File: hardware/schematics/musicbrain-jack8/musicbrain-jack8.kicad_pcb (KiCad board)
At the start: 2 copper layers, 20 x 125 mm, 10 parts, among them J1 SOCKET-BACK, J2 PJ398SM, J3 PJ398SM, J4 PJ398SM, J5 PJ398SM, J6 PJ398SM, J7 PJ398SM, J8 PJ398SM, J9 PJ398SM

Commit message: jack8/jack4 v1.2 + pot8front v1.1: koppel-standaard + 3D-socket-fix
- Front-koppeling gestandaardiseerd: 1x10-socket op x=116,5 (16,5 van west-
  rand), pin 1 op y=143,57 - identiek op jack8, jack4 en pot8front
- B-zijde-sockets nu in KiCads canonieke geflipte vorm (rot 180, lokale y
  genegeerd): koper ongewijzigd, maar het 3D-model staat nu OP de gatenrij
  i.p.v. ernaast gespiegeld
- PCB-papier naar A3 (borden vielen van A4-landscape af), silk-URL naar
  bordmidden (viel over de bordrand door center-justify)
- make_fab.sh: bordenlijst actueel (deprecated eruit, fronts erin),
  selectie-argument + gerber-zip-stap toegevoegd
- ERC/netcheck/DRC 0/0 op alle drie; fab + PDF's ververst

Co-Authored-By: Claude Fable 5 <noreply@anthropic.com>
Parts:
- moved J1 7.65 mm to (116.5, 143.6), turned to 180 degrees
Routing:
- net /CH8: track 43.7 -> 52.7 mm
- net /CH7: track 31.2 -> 40.2 mm
- net /CH6: track 18.8 -> 27.8 mm
- net /CH5: track 7.69 -> 15.3 mm
- net /CH4: track 20.1 -> 14.1 mm
- net /CH3: track 32.6 -> 26.6 mm
- net /CH2: track 45.1 -> 39.1 mm
- net /CH1: track 57.5 -> 51.5 mm
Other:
- board text added: "musicbrain.nl/hw/jack8 rev 1.2"
- board text removed: "musicbrain.nl/hw/jack8 rev 1.1"
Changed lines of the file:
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@@
   (generator_version "8.0")
   (general (thickness 1.6) (legacy_teardrops no))
-  (paper "A4")
+  (paper "A3")
   (title_block
     (title "MusicBrain jack8")
-    (date "2026-07-08")
-    (rev "1.1")
+    (date "2026-07-11")
+    (rev "1.2")
     (company "MusicBrain project")
   )
@@
   (footprint "MusicBrain:Header_1x10_backside"
     (layer "B.Cu")
-    (at 115 151.07)
+    (at 116.5 143.57 180)
     (descr "1x10 female socket op de ACHTERZIJDE (opening omlaag, naar de kaart)")
-    (property "Reference" "J1" (at 2.8 -2.2 0) (layer "B.SilkS")
+    (property "Reference" "J1" (at -2.8 2.2 0) (layer "B.SilkS")
       (effects (font (size 1 1) (thickness 0.15)) (justify mirror)))
-    (property "Value" "SOCKET-BACK" (at 0 25.86 0) (layer "B.Fab")
+    (property "Value" "SOCKET-BACK" (at 0 -25.86 0) (layer "B.Fab")
       (effects (font (size 1 1) (thickness 0.15)) (justify mirror)))
     (attr through_hole)
-    (fp_rect (start -1.6 -1.6) (end 1.6 24.46)
+    (fp_rect (start -1.6 -24.46) (end 1.6 1.6)
       (stroke (width 0.12) (type solid)) (fill no) (layer "B.SilkS"))
-    (fp_rect (start -1.8 -1.8) (end 1.8 24.66)
+    (fp_rect (start -1.8 -24.66) (end 1.8 1.8)
       (stroke (width 0.05) (type solid)) (fill no) (layer "B.CrtYd"))
-    (pad "1" thru_hole rect (at 0 0) (size 1.7 1.7) (drill 1.0) (layers "*.Cu" "*.Mask") (net 1 "GND"))
-    (pad "2" thru_hole oval (at 0 2.54) (size 1.7 1.7) (drill 1.0) (layers "*.Cu" "*.Mask") (net 3 "/CH1"))
-    (pad "3" thru_hole oval (at 0 5.08) (size 1.7 1.7) (drill 1.0) (layers "*.Cu" "*.Mask") (net 4 "/CH2"))
-    (pad "4" thru_hole oval (at 0 7.62) (size 1.7 1.7) (drill 1.0) (layers "*.Cu" "*.Mask") (net 5 "/CH3"))
-    (pad "5" thru_hole oval (at 0 10.16) (size 1.7 1.7) (drill 1.0) (layers "*.Cu" "*.Mask") (net 6 "/CH4"))
-    (pad "6" thru_hole oval (at 0 12.7) (size 1.7 1.7) (drill 1.0) (layers "*.Cu" "*.Mask") (net 7 "/CH5"))
-    (pad "7" thru_hole oval (at 0 15.24) (size 1.7 1.7) (drill 1.0) (layers "*.Cu" "*.Mask") (net 8 "/CH6"))
-    (pad "8" thru_hole oval (at 0 17.78) (size 1.7 1.7) (drill 1.0) (layers "*.Cu" "*.Mask") (net 9 "/CH7"))
-    (pad "9" thru_hole oval (at 0 20.32) (size 1.7 1.7) (drill 1.0) (layers "*.Cu" "*.Mask") (net 10 "/CH8"))
-    (pad "10" thru_hole oval (at 0 22.86) (size 1.7 1.7) (drill 1.0) (layers "*.Cu" "*.Mask") (net 1 "GND"))
+    (pad "1" thru_hole rect (at 0 -0 180) (size 1.7 1.7) (drill 1.0) (layers "*.Cu" "*.Mask") (net 1 "GND"))
+    (pad "2" thru_hole oval (at 0 -2.54 180) (size 1.7 1.7) (drill 1.0) (layers "*.Cu" "*.Mask") (net 3 "/CH1"))
+    (pad "3" thru_hole oval (at 0 -5.08 180) (size 1.7 1.7) (drill 1.0) (layers "*.Cu" "*.Mask") (net 4 "/CH2"))
+    (pad "4" thru_hole oval (at 0 -7.62 180) (size 1.7 1.7) (drill 1.0) (layers "*.Cu" "*.Mask") (net 5 "/CH3"))
+    (pad "5" thru_hole oval (at 0 -10.16 180) (size 1.7 1.7) (drill 1.0) (layers "*.Cu" "*.Mask") (net 6 "/CH4"))
+    (pad "6" thru_hole oval (at 0 -12.7 180) (size 1.7 1.7) (drill 1.0) (layers "*.Cu" "*.Mask") (net 7 "/CH5"))
+    (pad "7" thru_hole oval (at 0 -15.24 180) (size 1.7 1.7) (drill 1.0) (layers "*.Cu" "*.Mask") (net 8 "/CH6"))
+    (pad "8" thru_hole oval (at 0 -17.78 180) (size 1.7 1.7) (drill 1.0) (layers "*.Cu" "*.Mask") (net 9 "/CH7"))
+    (pad "9" thru_hole oval (at 0 -20.32 180) (size 1.7 1.7) (drill 1.0) (layers "*.Cu" "*.Mask") (net 10 "/CH8"))
+    (pad "10" thru_hole oval (at 0 -22.86 180) (size 1.7 1.7) (drill 1.0) (layers "*.Cu" "*.Mask") (net 1 "GND"))
     (model "${KICAD10_3DMODEL_DIR}/Connector_PinSocket_2.54mm.3dshapes/PinSocket_1x10_P2.54mm_Vertical.step"
       (offset (xyz 0 0 0)) (scale (xyz 1 1 1)) (rotate (xyz 0 0 0)))
@@
       (net 1 "GND"))
   )
-  (segment (start 115 153.61) (end 112.05 153.61) (width 0.25) (layer "F.Cu") (net 3))
-  (segment (start 112.05 153.61) (end 112.05 103.08) (width 0.25) (layer "F.Cu") (net 3))
-  (segment (start 112.05 103.08) (end 108 103.08) (width 0.25) (layer "F.Cu") (net 3))
-  (segment (start 115 156.15) (end 111.55 156.15) (width 0.25) (layer "F.Cu") (net 4))
-  (segment (start 111.55 156.15) (end 111.55 118.08) (width 0.25) (layer "F.Cu") (net 4))
-  (segment (start 111.55 118.08) (end 108 118.08) (width 0.25) (layer "F.Cu") (net 4))
-  (segment (start 115 158.69) (end 111.05 158.69) (width 0.25) (layer "F.Cu") (net 5))
-  (segment (start 111.05 158.69) (end 111.05 133.08) (width 0.25) (layer "F.Cu") (net 5))
-  (segment (start 111.05 133.08) (end 108 133.08) (width 0.25) (layer "F.Cu") (net 5))
-  (segment (start 115 161.23) (end 110.55 161.23) (width 0.25) (layer "F.Cu") (net 6))
-  (segment (start 110.55 161.23) (end 110.55 148.08) (width 0.25) (layer "F.Cu") (net 6))
-  (segment (start 110.55 148.08) (end 108 148.08) (width 0.25) (layer "F.Cu") (net 6))
-  (segment (start 115 163.77) (end 110.05 163.77) (width 0.25) (layer "F.Cu") (net 7))
-  (segment (start 110.05 163.77) (end 110.05 163.08) (width 0.25) (layer "F.Cu") (net 7))
-  (segment (start 110.05 163.08) (end 108 163.08) (width 0.25) (layer "F.Cu") (net 7))
-  (segment (start 115 166.31) (end 112.55 166.31) (width 0.25) (layer "F.Cu") (net 8))
-  (segment (start 112.55 166.31) (end 112.55 178.08) (width 0.25) (layer "F.Cu") (net 8))
+  (segment (start 116.5 146.11) (end 111.55 146.11) (width 0.25) (layer "F.Cu") (net 3))
+  (segment (start 111.55 146.11) (end 111.55 103.08) (width 0.25) (layer "F.Cu") (net 3))
+  (segment (start 111.55 103.08) (end 108 103.08) (width 0.25) (layer "F.Cu") (net 3))
+  (segment (start 116.5 148.65) (end 111.05 148.65) (width 0.25) (layer "F.Cu") (net 4))
+  (segment (start 111.05 148.65) (end 111.05 118.08) (width 0.25) (layer "F.Cu") (net 4))
+  (segment (start 111.05 118.08) (end 108 118.08) (width 0.25) (layer "F.Cu") (net 4))
+  (segment (start 116.5 151.19) (end 110.55 151.19) (width 0.25) (layer "F.Cu") (net 5))
+  (segment (start 110.55 151.19) (end 110.55 133.08) (width 0.25) (layer "F.Cu") (net 5))
+  (segment (start 110.55 133.08) (end 108 133.08) (width 0.25) (layer "F.Cu") (net 5))
+  (segment (start 116.5 153.73) (end 110.05 153.73) (width 0.25) (layer "F.Cu") (net 6))
+  (segment (start 110.05 153.73) (end 110.05 148.08) (width 0.25) (layer "F.Cu") (net 6))
+  (segment (start 110.05 148.08) (end 108 148.08) (width 0.25) (layer "F.Cu") (net 6))
+  (segment (start 116.5 156.27) (end 112.05 156.27) (width 0.25) (layer "F.Cu") (net 7))
+  (segment (start 112.05 156.27) (end 112.05 163.08) (width 0.25) (layer "F.Cu") (net 7))
+  (segment (start 112.05 163.08) (end 108 163.08) (width 0.25) (layer "F.Cu") (net 7))
+  (segment (start 116.5 158.81) (end 112.55 158.81) (width 0.25) (layer "F.Cu") (net 8))
+  (segment (start 112.55 158.81) (end 112.55 178.08) (width 0.25) (layer "F.Cu") (net 8))
   (segment (start 112.55 178.08) (end 108 178.08) (width 0.25) (layer "F.Cu") (net 8))
-  (segment (start 115 168.85) (end 113.05 168.85) (width 0.25) (layer "F.Cu") (net 9))
-  (segment (start 113.05 168.85) (end 113.05 193.08) (width 0.25) (layer "F.Cu") (net 9))
+  (segment (start 116.5 161.35) (end 113.05 161.35) (width 0.25) (layer "F.Cu") (net 9))
+  (segment (start 113.05 161.35) (end 113.05 193.08) (width 0.25) (layer "F.Cu") (net 9))
   (segment (start 113.05 193.08) (end 108 193.08) (width 0.25) (layer "F.Cu") (net 9))
-  (segment (start 115 171.39) (end 113.55 171.39) (width 0.25) (layer "F.Cu") (net 10))
-  (segment (start 113.55 171.39) (end 113.55 208.08) (width 0.25) (layer "F.Cu") (net 10))
+  (segment (start 116.5 163.89) (end 113.55 163.89) (width 0.25) (layer "F.Cu") (net 10))
+  (segment (start 113.55 163.89) (end 113.55 208.08) (width 0.25) (layer "F.Cu") (net 10))
   (segment (start 113.55 208.08) (end 108 208.08) (width 0.25) (layer "F.Cu") (net 10))
   (segment (start 108 111.38) (end 103.5 111.38) (width 0.3) (layer "F.Cu") (net 2))
@@
     (stroke (width 0.1) (type default)) (fill none)
     (layer "Edge.Cuts"))
-  (gr_text "musicbrain.nl/hw/jack8 rev 1.1" (at 101.3 223 90) (layer "F.SilkS")
+  (gr_text "musicbrain.nl/hw/jack8 rev 1.2" (at 101.3 162.5 90) (layer "F.SilkS")
     (effects (font (size 1 1) (thickness 0.15))))
   (zone (net 1) (net_name "GND") (layer "F.Cu")

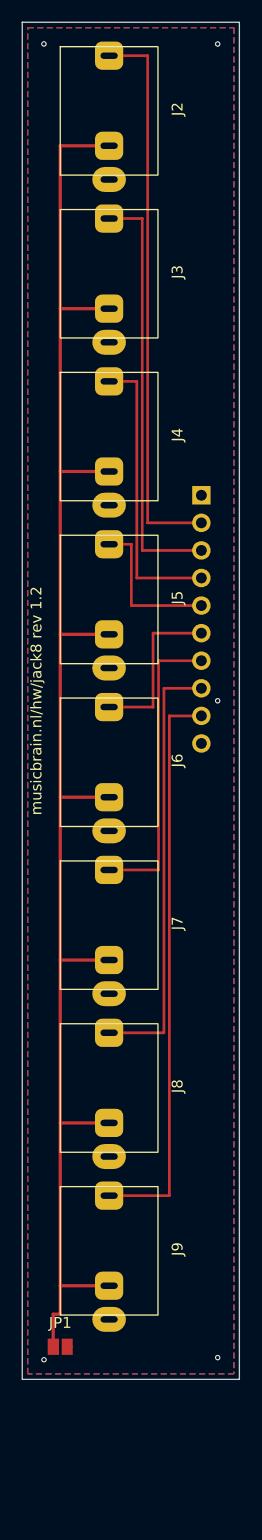
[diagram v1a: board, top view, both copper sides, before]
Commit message: jack8/jack4 gen 2: steek 13,75; jack8 110 mm met socket op het hart
- jacksteek 15 -> 13,75 (4 HP-front, = pot8front); jack8 125 -> 110 mm
  (past nu tussen de rails); socket op HY0 143,57 = exact gecentreerd
- jack4 alleen de steek (kabelbord aan de hub-DAC, centrering irrelevant)
- Thonkiconn-pads in y geslankt (tip 1,8 / sleeve 1,5; annular >= 0,45,
  slot 1,6x0,6) - op 13,75 raakten de gen-1-pads elkaar; courtyard strak
  om body+pads (was 15-steek-maat)
- jackkolom op de pad-envelop gecentreerd (envelop is 0,7 asymmetrisch);
  rand-marge expliciet 0,3 (JLC-minimum) in de .kicad_pro
- JP1 naar BY1-1,5 + NORM-rail doorgetrokken; hechtvia uit de JP1-zone
- beide: ERC 0, netcheck OK, DRC 0/0

Co-Authored-By: Claude Fable 5 <noreply@anthropic.com>
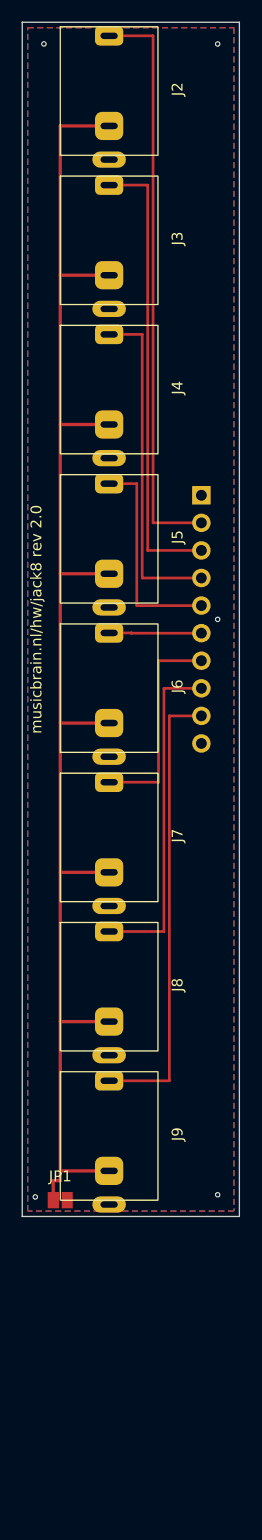
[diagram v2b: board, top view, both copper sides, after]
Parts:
- moved JP1 13.5 mm to (103.5, 208.5)
- moved J9 10.6 mm to (108.0, 202.4)
- moved J8 9.33 mm to (108.0, 188.7)
- moved J7 8.08 mm to (108.0, 174.9)
- moved J6 6.83 mm to (108.0, 161.2)
- moved J5 5.58 mm to (108.0, 147.4)
- moved J4 4.33 mm to (108.0, 133.7)
- moved J3 3.08 mm to (108.0, 119.9)
- moved J2 1.83 mm to (108.0, 106.2)
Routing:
- net /NORM: track 147.3 -> 135.6 mm
- net /CH8: track 52.7 -> 42.1 mm
- net /CH7: track 40.2 -> 30.9 mm
- net /CH6: track 27.8 -> 19.7 mm
- net /CH5: track 15.3 -> 8.52 mm
- net /CH4: track 14.1 -> 19.7 mm
- net /CH3: track 26.6 -> 30.9 mm
- net /CH2: track 39.1 -> 42.2 mm
- net /CH1: track 51.5 -> 53.4 mm
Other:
- board size 20 x 125 mm -> 20 x 110 mm
- board text added: "musicbrain.nl/hw/jack8 rev 2.0"
- board text removed: "musicbrain.nl/hw/jack8 rev 1.2"
